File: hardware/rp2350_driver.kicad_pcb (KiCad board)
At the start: 6 copper layers, 76 x 46.4 mm, 291 parts, among them J1 XT30, J10 Power Output, J11 CAN2 PLUG, J12 Conn_01x06, J2 XT30, J3 USB_C_Receptacle_USB2.0, J4 SM03B-SRSS-TB, J5 Estop Conn, J6 SM03B-SRSS-TB, J7 Conn_01x03, J8 Conn_01x03, J9 XT30, Q1 Q_PNP_BEC, Q2 Q_PNP_BEC, Q3 Q_PNP_BEC, Q4 Q_PNP_BEC, Q5 Q_NMOS_GDS, SW1 Button, SW2 Button, U1 EG3113, U10 INA240A1D, U101 FUSB302BMPX, U11 USBLC6-2P6, U12 EG3113, U13 TS5A3159DCK, U14 TS5A3159DCK, U15 TS5A3159DCK, U16 CA-IS3052CG, U17 TS5A3159DCK, U18 SIT3088ETK, U19 SIT3088ETK, U20 SIT3088ETK, U21 SIT3088ETK, U22 TS5A3159DCK, U23 TS5A3159DCK, U24 TS5A3159DCK, U25 TS5A3159DCK, U26 TS5A3159DCK, U27 TS5A3159DCK, U28 XL7005A, U29 LM74700, U3 W25Q16JV, U4 SPX3819M5-L-3-3, U5 INA240A1D, U6 EG3113, U7 EG3113, U8 RP2350_80QFN, U9 INA240A1D, Y1 ABM8-272-T3

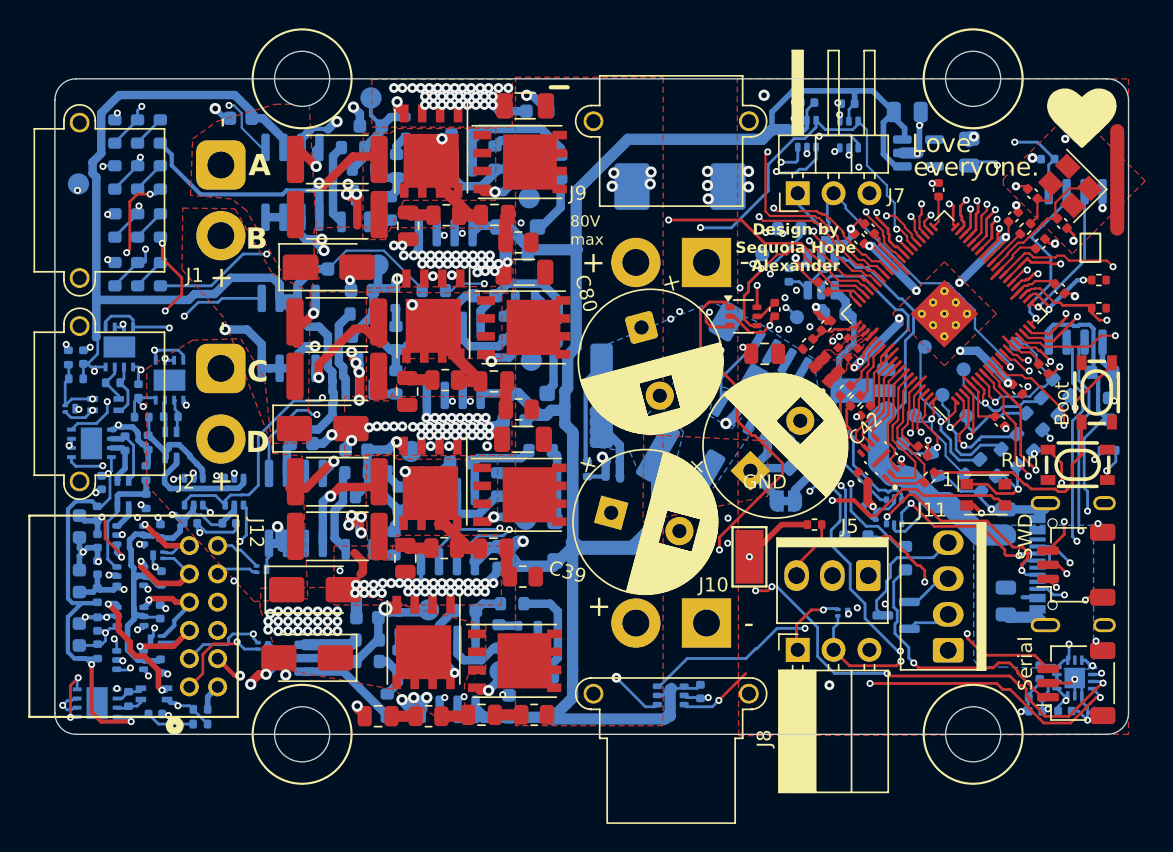
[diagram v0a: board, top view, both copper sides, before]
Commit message: board: rev-A copper + rev-B nets and parts + Tier A swaps (rev-b-lean)
Built from the rev-A-fab board in two stages, both logged:

  1  tools/revb/sync_pcb.py --apply   F-27/F-39 exactly as on rev-b-fixes:
     U29 -> LTC4359 MSOP-8, Q5 -> PowerPAK SO-8, D31 added, C79 removed,
     U11 pad 5 -> +3V3, TP15/TP17 shoved; 84 segments ripped (VBUS,
     Net-(JP1-A), Net-(Q5-G)) and left as airwires for a 1.5 mm hand route
  2  tools/lean/build_lean.py, driven by the schematic netlist:
     A  9 net renames (ENC_x_TRX_A/B, TERM_SW) - copper keeps its identity
     B  R82-R85 pad 2 -> TERM_x_R, D1 pad 3 -> LED_VDD; the A-line passes
        through each resistor pad, so 16 segments are cut (4 airwires)
     C  15 value-only changes (BSC030N08NS5, SMDJ64A/SMAJ64A)
     D  182 footprint swaps to the parts:* library (F-43 shrink, snubbers,
        test points, SC-70, tight courtyards, WS2812B-2020); 70 stubs
        re-bridge copper to the smaller pads; 8 foreign tracks/vias that
        KiCad's shape test says now collide are ripped (C_SENSE between
        C40's pads, GND_ISO between R53's, the LED's GND/Vdrive feed)
     E  33 new parts: 25 placed clean (rev-b-fixes pose or within 3 mm),
        7 parked below the board edge - U30 U32 U33 R97 R98 R100 C110,
        the encoder corner has no room (F-44). No rev-A copper ripped
        for a new part.
     F  schematic paths set from the netlist for all 323 footprints
  +  .kicad_pro: netclasses "usb_5A" (1.5 mm; VBUS, Net-(JP1-A)) and
     "power" (0.6 mm; +3V3) - the old assignment pointed at a class that
     did not exist, which is why every router drew VBUS at 0.2 mm

Result vs rev-A-fab: 3876 of 3984 segments and 488 of 493 vias
bit-identical, zone outlines untouched, outline unchanged (76 x 46.4).
check_sync.py: IN SYNC. DRC: 1 clearance error (R83 pad 2 vs FL1 pad 4,
a placement fix), 0 shorts, 7 courtyard overlaps (rev A: 10), 30
dangling ends from the rips, 103 unconnected = the routing worklist.

Co-Authored-By: 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
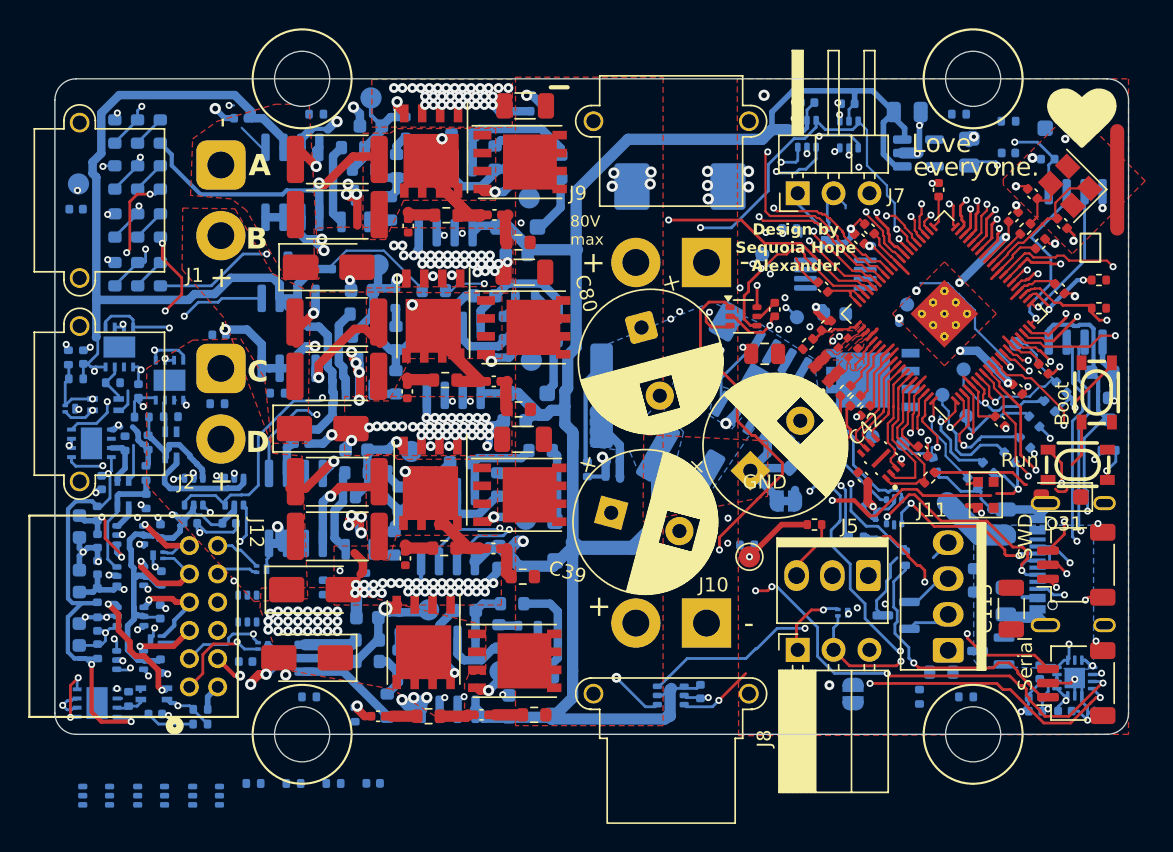
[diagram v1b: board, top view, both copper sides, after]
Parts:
- removed C79: 100n, Capacitor_SMD:C_0402_1005Metric
- added C110: 100n, parts:C_0402_1005Metric_JLC, B.Cu at (135.0, 131.9)
- added C111: 100n, parts:C_0402_1005Metric_JLC, B.Cu at (126.0, 123.2)
- added C112: 100n, parts:C_0402_1005Metric_JLC, B.Cu at (124.1, 100.1)
- added C113: 100n, parts:C_0402_1005Metric_JLC, B.Cu at (114.0, 91.2)
- added C114: 100n, parts:C_0402_1005Metric_JLC, B.Cu at (180.0, 87.2)
- added C115: 1n 2kV, Capacitor_SMD:C_1206_3216Metric, F.Cu at (180.2, 119.5)
- added D30: DSS110, Diode_SMD:D_SOD-123F, B.Cu at (184.0, 85.5)
- added D31: SMF24A, Diode_SMD:D_SOD-123F, F.Cu at (183.7, 111.6)
- added JP2: Jumper_2_Open, Jumper:SolderJumper-2_P1.3mm_Open_RoundedPad1.0x1.5mm, B.Cu at (169.0, 125.5)
- added Q6: 2N7002, Package_TO_SOT_SMD:SOT-23, B.Cu at (178.8, 122.5)
- added R100: 10k, parts:R_0402_1005Metric_JLC, B.Cu at (132.2, 131.9)
- added R101: 100k, parts:R_0402_1005Metric_JLC, B.Cu at (134.5, 117.5)
- added R102: 100k, parts:R_0402_1005Metric_JLC, B.Cu at (131.5, 118.0)
- added R103: 100k, parts:R_0402_1005Metric_JLC, B.Cu at (143.8, 107.8)
- added R104: 100k, parts:R_0402_1005Metric_JLC, B.Cu at (128.2, 104.2)
- added R105: 100k, parts:R_0402_1005Metric_JLC, B.Cu at (133.8, 127.0)
- added R106: 100k, parts:R_0402_1005Metric_JLC, B.Cu at (130.5, 125.8)
- added R107: 100k, parts:R_0402_1005Metric_JLC, B.Cu at (129.0, 95.0)
- added R108: 100k, parts:R_0402_1005Metric_JLC, B.Cu at (161.5, 115.0)
- added R109: 100k, parts:R_0402_1005Metric_JLC, B.Cu at (131.0, 84.5)
- added R110: 100k, parts:R_0402_1005Metric_JLC, B.Cu at (173.7, 125.7)
- added R111: 100k, parts:R_0402_1005Metric_JLC, B.Cu at (177.0, 125.8)
- added R112: 100k, parts:R_0402_1005Metric_JLC, B.Cu at (176.5, 84.5)
- added R113: 10k, parts:R_0402_1005Metric_JLC, B.Cu at (180.0, 85.0)
- added R114: 120R, Resistor_SMD:R_0603_1608Metric, B.Cu at (177.6, 117.5)
- added R115: 100R, Resistor_SMD:R_0603_1608Metric, B.Cu at (175.2, 124.0)
- added R97: 10k, parts:R_0402_1005Metric_JLC, B.Cu at (126.6, 131.9)
- added R98: 10k, parts:R_0402_1005Metric_JLC, B.Cu at (129.4, 131.9)
- added R99: 10k, parts:R_0402_1005Metric_JLC, B.Cu at (124.0, 105.0)
- added U30: TS5A3159DCK, parts:SOT-363_SC-70-6_JLC, B.Cu at (115.4, 132.7)
- added U31: TS5A3159DCK, parts:SOT-363_SC-70-6_JLC, B.Cu at (126.1, 119.5)
- added U32: TS5A3159DCK, parts:SOT-363_SC-70-6_JLC, B.Cu at (119.3, 132.7)
- added U33: TS5A3159DCK, parts:SOT-363_SC-70-6_JLC, B.Cu at (123.2, 132.7)
- AH1, AL1, BH1, BL1, CH1, CH2, CL1, CL2: value MOSFETSO-8 -> BSC030N08NS5
- C10, C15, C2, C23, C27, C28, C31, C36, C48, C51, C55, C57, C58, C6, C69, C70, C75, C78, C81: footprint Capacitor_SMD:C_0603_1608Metric -> parts:C_0603_1608Metric_JLC
- C105, C106, C12, C47, C5: footprint Capacitor_SMD:C_0805_2012Metric -> parts:C_0805_2012Metric_JLC
- C107, C108, C13, C14, C20, C21, C22, C24, C3, C30, C32, C35, C37, C38, C4, C41, C43, C45, C46, C49, C50, C52, C56, C59, C60, C61, C62, C63, C64, C65, C66, C67, C68, C71, C72, C73, C74, C76, C77: footprint Capacitor_SMD:C_0402_1005Metric -> parts:C_0402_1005Metric_JLC
- C16, C19, C29, C40: footprint Capacitor_SMD:C_0603_1608Metric -> parts:C_0402_1005Metric_JLC
- C25, C26, C33, C34, C53, C54, C7, C9: footprint Capacitor_SMD:C_0805_2012Metric -> parts:C_0402_1005Metric_JLC
- D1: footprint RP2040_minimal:LED_WS2812_3528_3.5x2.8mm_P1.5mm -> parts:LED_WS2812B-2020_PLCC4_2.0x2.0mm_MotorBuck
- D13, D17, D21, D9: value SMAJ51A -> SMAJ64A
- D5: value SMDJ85A -> SMDJ64A
- Q5: value Q_NMOS_GDS -> E100N4P0HL1; footprint Package_TO_SOT_SMD:SOT-89-3 -> parts:PowerPAK_SO-8_123
- R1, R2, R21, R22, R35, R36, R49, R53, R54, R65, R66: footprint Resistor_SMD:R_0603_1608Metric -> parts:R_0402_1005Metric_JLC
- R10, R11, R12, R13, R14, R15, R25, R27, R28, R29, R30, R31, R33, R41, R42, R43, R44, R45, R46, R47, R59, R60, R61, R62, R63, R64, R67, R68, R69, R70, R71, R72, R73, R74, R75, R76, R77, R78, R79, R9, TH1: footprint Resistor_SMD:R_0603_1608Metric -> parts:R_0603_1608Metric_JLC
- R17, R18, R37, R38, R48, R52, R80, R81: footprint Resistor_SMD:R_0805_2012Metric -> parts:R_0603_1608Metric_JLC
- R24, R26, R32, R34, R5, R50, R51, R57, R58, R6, R8, R82, R83, R84, R85, R86, R87, R88, R89, R90, R91, R92, R93, R94, R95, R96: footprint Resistor_SMD:R_0402_1005Metric -> parts:R_0402_1005Metric_JLC
- TP12, TP13, TP14, TP15, TP16, TP17, TP18, TP19, TP20: footprint TestPoint:TestPoint_Pad_D1.0mm -> parts:TestPoint_Pad_D1.0mm_no_courtyard
- TP8: footprint TestPoint:TestPoint_Keystone_5019_Minature -> parts:TestPoint_Pad_D1.5mm_no_courtyard
- U13, U14, U15, U17, U22, U23, U24, U25, U26, U27: footprint Package_TO_SOT_SMD:SOT-363_SC-70-6 -> parts:SOT-363_SC-70-6_JLC
- U29: value LM74700 -> LTC4359CMS8; footprint Package_TO_SOT_SMD:SOT-23-6 -> Package_SO:MSOP-8_3x3mm_P0.65mm
- moved TP15 3.35 mm to (170.4, 107.3)
- moved TP17 3.25 mm to (172.8, 98.0)
- moved Q5 1.25 mm to (170.4, 103.3)
- moved U29 1.00 mm to (167.7, 95.8), turned to 0 degrees
- turned D1 to -90 degrees
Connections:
- net Net-(U18-B) renamed /ENC_A_TRX_B
- net Net-(U19-B) renamed /ENC_B_TRX_B
- net Net-(U20-B) renamed /ENC_C_TRX_B
- net Net-(U21-B) renamed /ENC_D_TRX_B
- net Net-(U8-GPIO38) renamed /TERM_SW
- D1 pad 3: Vdrive -> /LED_VDD
- FL1 pad 4: Net-(U19-A) -> /ENC_B_TRX_A
- FL2 pad 4: Net-(U18-A) -> /ENC_A_TRX_A
- FL3 pad 4: Net-(U20-A) -> /ENC_C_TRX_A
- FL4 pad 4: Net-(U21-A) -> /ENC_D_TRX_A
- Q5 pad 1: Net-(Q5-G) -> VBUS
- Q5 pad 2: Net-(JP1-A) -> Net-(Q5-G)
- Q5 pad 3: VBUS -> Net-(JP1-A)
- R82 pad 2: Net-(U18-A) -> /TERM_A_R
- R83 pad 2: Net-(U19-A) -> /TERM_B_R
- R84 pad 2: Net-(U20-A) -> /TERM_C_R
- R85 pad 2: Net-(U21-A) -> /TERM_D_R
- U11 pad 5: VBUS -> +3V3
- U18 pad 6: Net-(U18-A) -> /ENC_A_TRX_A
- U19 pad 6: Net-(U19-A) -> /ENC_B_TRX_A
- U20 pad 6: Net-(U20-A) -> /ENC_C_TRX_A
- U21 pad 6: Net-(U21-A) -> /ENC_D_TRX_A
- U29 pad 1: Net-(U29-VCAP) -> Net-(Q5-G)
- U29 pad 2: GND -> VBUS
- U29 pad 3: VBUS -> unconnected-(U29-NC-Pad3)
- U29 pad 4: Net-(JP1-A) -> VBUS
- U29 pad 5: Net-(Q5-G) -> VBUS
- U29 pad 6: VBUS -> GND
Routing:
- net VBUS: track 41.1 -> 6.21 mm
- net Net-(JP1-A): track 23.8 -> 0.78 mm
- net Net-(Q5-G): track 12.4 -> 0.00 mm
- net +1V1: track 29.2 -> 20.3 mm, vias 9 -> 7
- net /RXI_INTERBOARD_1: track 22.5 -> 15.0 mm
- net GND: track 223.5 -> 229.2 mm, vias 238 -> 236
- net B_PWM_H: track 49.4 -> 44.4 mm
- net Net-(U18-A): track 4.57 -> 0.00 mm
- net A_PWM_L\: track 48.7 -> 44.3 mm
- net /~{USB_BOOT}: track 15.2 -> 11.1 mm
- net Net-(U21-A): track 3.81 -> 0.00 mm
- net +3V3: track 256.6 -> 259.3 mm
- net /ENC_A_TRX_A: track 0.00 -> 2.64 mm
- net /TH1_SENSE: track 18.9 -> 16.3 mm
- net GND_ISO: track 30.3 -> 27.8 mm
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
